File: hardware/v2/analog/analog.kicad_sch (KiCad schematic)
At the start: 24 parts, among them J1 Conn_Coaxial, K1 Relay_SPDT, Q1 BC547, U1 CD4051B, U2 TL081, U3 TL431LP

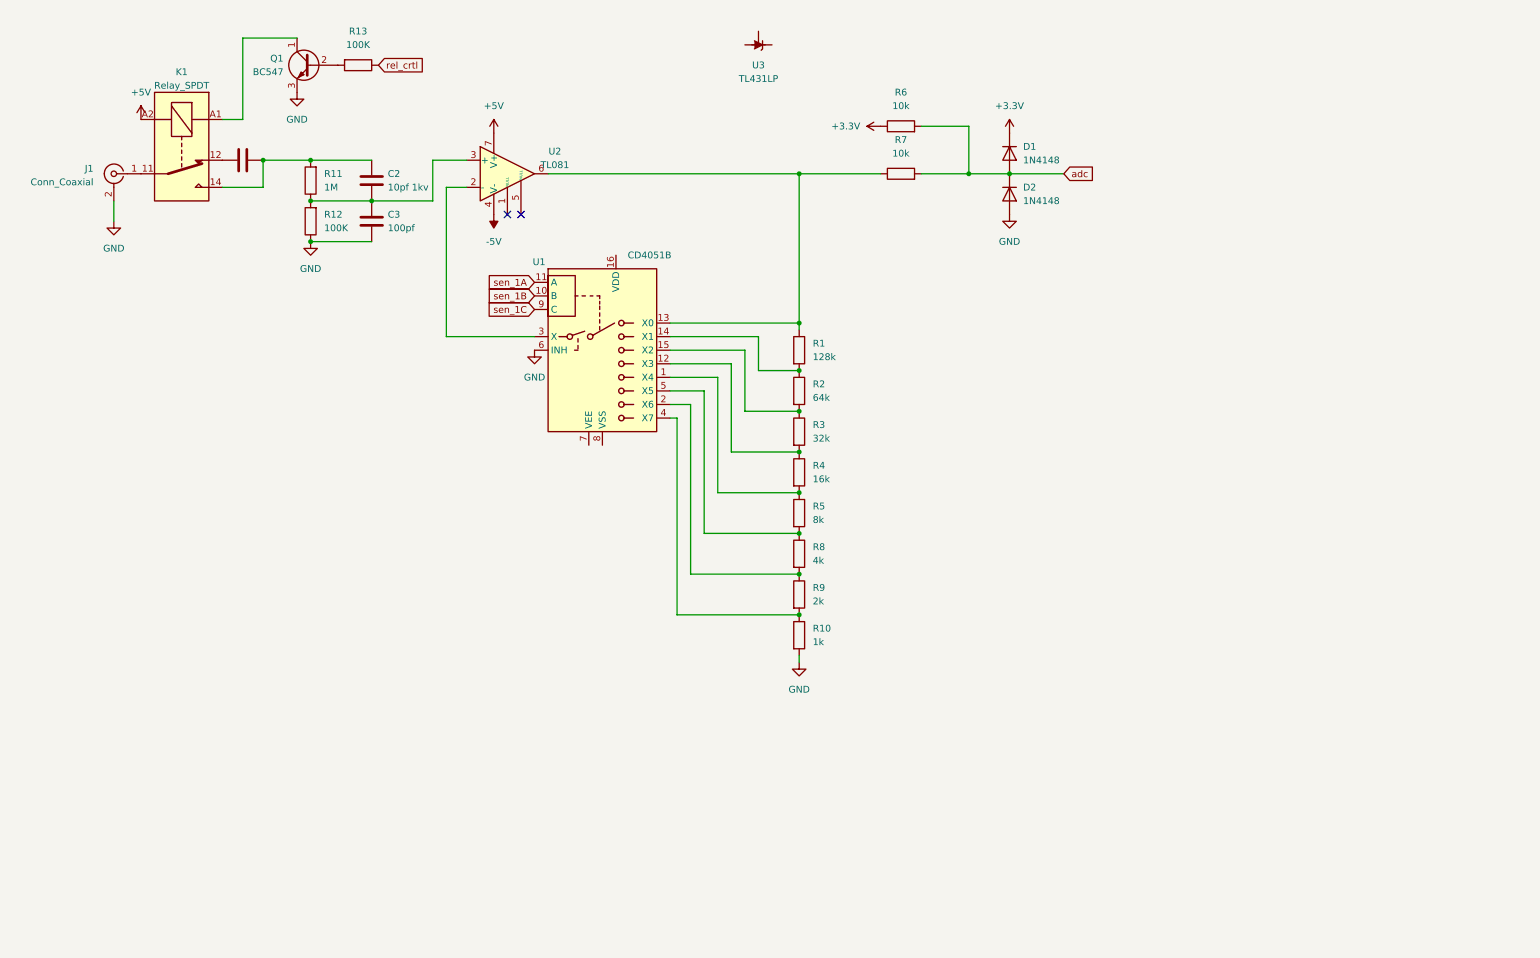
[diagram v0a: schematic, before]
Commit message: Analog Part Changes
EN : Schematic is Modified
FA : نقشه مدار تغییر یافت
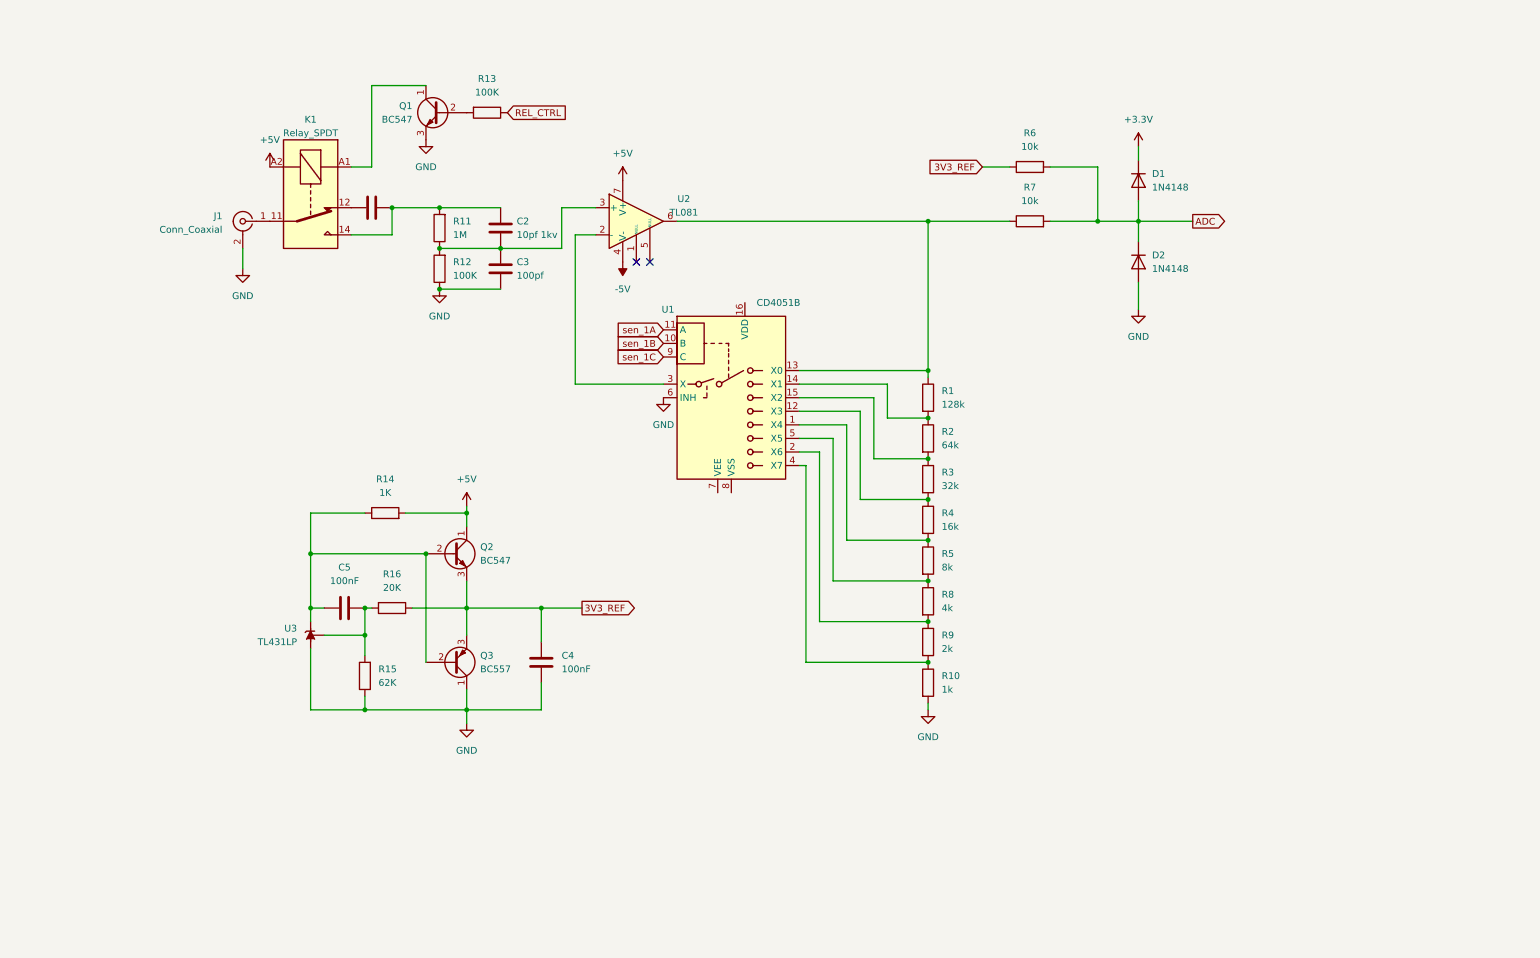
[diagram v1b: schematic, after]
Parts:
- added C4, C5: 100nF, symbol Custom_Device:C
- added Q2: BC547, Package_TO_SOT_THT:TO-92_Inline, symbol Transistor_BJT:BC547
- added Q3: BC557, Package_TO_SOT_THT:TO-92_Inline, symbol Transistor_BJT:BC557
- added R14: 1K, symbol Custom_Device:R
- added R15: 62K, symbol Custom_Device:R
- added R16: 20K, symbol Custom_Device:R
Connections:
- net +3.3V: no longer R6.1
- net +5V: now also Q2.1 (C), R14.2
- net GND: now also U3.2 (A), C4.2, Q3.1 (C), R15.1
- net at U3.1 (REF): now also C5.2, R15.2, R16.2
- net at U3.3 (K): now also C5.1, Q2.2 (B), Q3.2 (B), R14.1
- net adc renamed ADC
- net rel_crtl renamed REL_CTRL
- new net 3V3_REF: C4.1, Q2.3 (E), Q3.3 (E), R16.1, R6.1
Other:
- company: (none) -> epsi1on + HS6502 + axiom
- title: (none) -> Analog Part of RP-Pi-Oscope
- moved on the sheet: C2, C3, D1, D2, J1, K1, Q1, R1, R10, R11, R12, R13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

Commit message: update
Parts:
- added C6, C8: 100nf, symbol Device:C
- added C7: 47uF, symbol Device:C_Polarized
- added C9: 220uF, symbol Device:C_Polarized
- added D3, D4, D5, D6: 1n4148, symbol Device:D
- added Q4: BC547, Package_TO_SOT_THT:TO-92_Inline, symbol Transistor_BJT:BC547
- added Q5: BC557, Package_TO_SOT_THT:TO-92_Inline, symbol Transistor_BJT:BC557
- added R17, R18: 10k, symbol Device:R
- R13: value 100K -> 1K
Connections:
- net +5V: now also Q4.1 (C), R17.1
- net -5V: now also C9.2, D6.2 (A), R18.2
- net GND: now also C7.1, C9.1, D3.1 (K), Q5.1 (C)
- new net: C6.2, D3.2 (A), D4.1 (K)
- new net: C6.1, C8.1, Q4.3 (E), Q5.3 (E)
- new net: C7.2, D4.2 (A), D5.1 (K)
- new net: C8.2, D5.2 (A), D6.1 (K)
- new net V_inv_FB: R17.2, R18.1
- new net inv-pwm: Q4.2 (B), Q5.2 (B)
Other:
- moved on the sheet: C2, C3, C4, C5, D1, D2, J1, K1, Q1, Q2, Q3, R1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

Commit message: update
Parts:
- added TP1: 1khz, symbol Connector:TestPoint
- added TP2: GNDA, symbol Connector:TestPoint
- added TP3: 3v3, symbol Connector:TestPoint
- added U4: Pico, RPi_Pico:RPi_Pico_SMD_TH, symbol MCU_RaspberryPi_and_Boards:Pico
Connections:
- net 3V3_REF is gone; now on net +3.3VA: C4.1, Q2.3 (E), Q3.3 (E), R16.1, R6.1
- net +5V: now also U1.16 (VDD), U4.40 (VBUS)
- net -5V: now also U1.7 (VEE)
- net GND: now also U1.8 (VSS), U4.13 (GND), U4.18 (GND), U4.23 (GND), U4.28 (GND), U4.3 (GND), U4.38 (GND), U4.8 (GND); no longer D2.2 (A)
- net +3.3V renamed +3.3VA
- net +3.3VA: now also TP3.1, U4.35 (ADC_VREF)
- net ADC renamed pico-adc
- net pico-adc: now also U4.31 (GPIO26_ADC0)
- new net GNDA: D2.2 (A), TP2.1, U4.33 (AGND)

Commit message: update
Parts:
- removed K1: Relay_SPDT, symbol Relay:Relay_SPDT
- added K2: SANYOU_SRD_Form_C, Relay_THT:Relay_SPDT_SANYOU_SRD_Series_Form_C, symbol Relay:SANYOU_SRD_Form_C
- C1: footprint (none) -> Capacitor_THT:C_Disc_D6.0mm_W2.5mm_P5.00mm
- C2, C3, C4, C5, C7: footprint (none) -> Capacitor_THT:C_Disc_D7.5mm_W5.0mm_P7.50mm
- C6, C8: footprint (none) -> Capacitor_THT:C_Disc_D7.5mm_W2.5mm_P5.00mm
- C9: footprint (none) -> Capacitor_THT:CP_Radial_D10.0mm_P5.00mm
- D3, D4, D5, D6: footprint (none) -> Diode_THT:D_DO-35_SOD27_P7.62mm_Horizontal
- J1: footprint (none) -> Connector_Coaxial:BNC_Amphenol_B6252HB-NPP3G-50_Horizontal
- R1, R10, R11, R12, R13, R14, R15, R16, R17, R18, R2, R3, R4, R5, R6, R7, R8, R9: footprint (none) -> Resistor_THT:R_Axial_DIN0309_L9.0mm_D3.2mm_P12.70mm_Horizontal
- TP1, TP2, TP3: footprint (none) -> TestPoint:TestPoint_Pad_3.0x3.0mm
- U1, U2: footprint (none) -> Package_DIP:DIP-8_W7.62mm_LongPads
- U4: footprint RPi_Pico:RPi_Pico_SMD_TH -> MCU_RaspberryPi_and_Boards:RPi_Pico_SMD_TH
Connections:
- net +5V: now also K2.2
- net at C1.2, C2.2, R11.2: now also K2.3
- net at Q1.1 (C): now also K2.5
- net at J1.1 (In): now also K2.1
- net at C1.1: now also K2.4

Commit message: update 2
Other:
- moved on the sheet: TP1, TP2, TP3
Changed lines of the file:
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@@
 	(symbol
 		(lib_id "Connector:TestPoint")
-		(at 238.76 153.67 0)
+		(at 238.76 157.48 0)
 		(unit 1)
 		(exclude_from_sim no)
@@
 		(fields_autoplaced yes)
 		(property "Reference" "TP3"
-			(at 241.3 149.0979 0)
+			(at 241.3 152.9079 0)
 			(effects
 				(font
@@
 		)
 		(property "Value" "3v3"
-			(at 241.3 151.6379 0)
+			(at 241.3 155.4479 0)
 			(effects
 				(font
@@
 		)
 		(property "Footprint" "TestPoint:TestPoint_Pad_3.0x3.0mm"
-			(at 243.84 153.67 0)
+			(at 243.84 157.48 0)
 			(effects
 				(font
@@
 		)
 		(property "Datasheet" "~"
-			(at 243.84 153.67 0)
+			(at 243.84 157.48 0)
 			(effects
 				(font
@@
 		)
 		(property "Description" "test point"
-			(at 238.76 153.67 0)
+			(at 238.76 157.48 0)
 			(effects
 				(font
@@
 	(symbol
 		(lib_id "power:GNDA")
-		(at 223.52 153.67 0)
+		(at 223.52 157.48 0)
 		(unit 1)
 		(exclude_from_sim no)
@@
 		(fields_autoplaced yes)
 		(property "Reference" "#PWR033"
-			(at 223.52 160.02 0)
+			(at 223.52 163.83 0)
 			(effects
 				(font
@@
 		)
 		(property "Value" "GNDA"
-			(at 223.52 158.75 0)
+			(at 223.52 162.56 0)
 			(effects
 				(font
@@
 		)
 		(property "Footprint" ""
-			(at 223.52 153.67 0)
+			(at 223.52 157.48 0)
 			(effects
 				(font
@@
 		)
 		(property "Datasheet" ""
-			(at 223.52 153.67 0)
+			(at 223.52 157.48 0)
 			(effects
 				(font
@@
 		)
 		(property "Description" "Power symbol creates a global label with name \"GNDA\" , analog ground"
-			(at 223.52 153.67 0)
+			(at 223.52 157.48 0)
 			(effects
 				(font
@@
 	(symbol
 		(lib_id "Connector:TestPoint")
-		(at 223.52 153.67 0)
+		(at 223.52 157.48 0)
 		(unit 1)
 		(exclude_from_sim no)
@@
 		(fields_autoplaced yes)
 		(property "Reference" "TP2"
-			(at 226.06 149.0979 0)
+			(at 226.06 152.9079 0)
 			(effects
 				(font
@@
 		)
 		(property "Value" "GNDA"
-			(at 226.06 151.6379 0)
+			(at 226.06 155.4479 0)
 			(effects
 				(font
@@
 		)
 		(property "Footprint" "TestPoint:TestPoint_Pad_3.0x3.0mm"
-			(at 228.6 153.67 0)
+			(at 228.6 157.48 0)
 			(effects
 				(font
@@
 		)
 		(property "Datasheet" "~"
-			(at 228.6 153.67 0)
+			(at 228.6 157.48 0)
 			(effects
 				(font
@@
 		)
 		(property "Description" "test point"
-			(at 223.52 153.67 0)
+			(at 223.52 157.48 0)
 			(effects
 				(font
@@
 	(symbol
 		(lib_id "Connector:TestPoint")
-		(at 207.01 153.67 0)
+		(at 207.01 157.48 0)
 		(unit 1)
 		(exclude_from_sim no)
@@
 		(fields_autoplaced yes)
 		(property "Reference" "TP1"
-			(at 209.55 149.0979 0)
+			(at 209.55 152.9079 0)
 			(effects
 				(font
@@
 		)
 		(property "Value" "1khz"
-			(at 209.55 151.6379 0)
+			(at 209.55 155.4479 0)
 			(effects
 				(font
@@
 		)
 		(property "Footprint" "TestPoint:TestPoint_Pad_3.0x3.0mm"
-			(at 212.09 153.67 0)
+			(at 212.09 157.48 0)
 			(effects
 				(font
@@
 		)
 		(property "Datasheet" "~"
-			(at 212.09 153.67 0)
+			(at 212.09 157.48 0)
 			(effects
 				(font
@@
 		)
 		(property "Description" "test point"
-			(at 207.01 153.67 0)
+			(at 207.01 157.48 0)
 			(effects
 				(font
@@
 	(symbol
 		(lib_id "power:+3.3VA")
-		(at 238.76 153.67 180)
+		(at 238.76 157.48 180)
 		(unit 1)
 		(exclude_from_sim no)
@@
 		(dnp no)
 		(property "Reference" "#PWR034"
-			(at 238.76 149.86 0)
+			(at 238.76 153.67 0)
 			(effects
 				(font
@@
 		)
 		(property "Value" "+3.3VA"
-			(at 238.506 159.258 0)
+			(at 238.506 163.068 0)
 			(effects
 				(font
@@
 		)
 		(property "Footprint" ""
-			(at 238.76 153.67 0)
+			(at 238.76 157.48 0)
 			(effects
 				(font
@@
 		)
 		(property "Datasheet" ""
-			(at 238.76 153.67 0)
+			(at 238.76 157.48 0)
 			(effects
 				(font
@@
 		)
 		(property "Description" "Power symbol creates a global label with name \"+3.3VA\""
-			(at 238.76 153.67 0)
+			(at 238.76 157.48 0)
 			(effects
 				(font
